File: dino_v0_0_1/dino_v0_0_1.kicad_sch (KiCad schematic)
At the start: 27 parts, among them Q1 Write Button Gate, U1 Quad AND

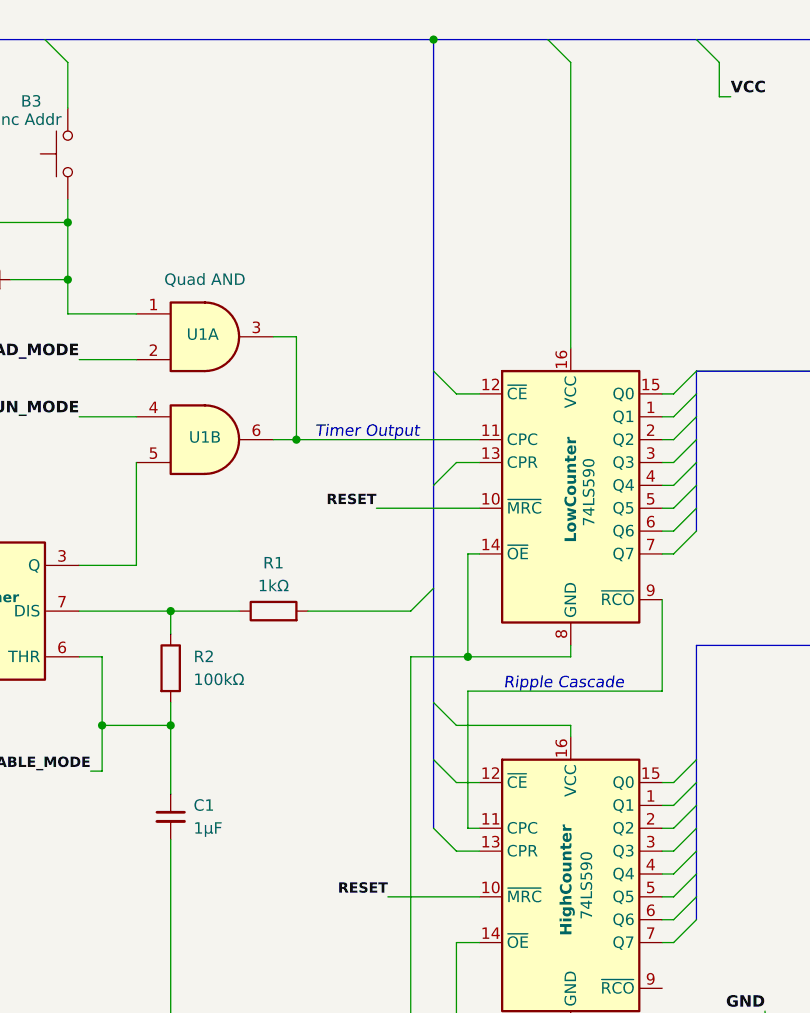
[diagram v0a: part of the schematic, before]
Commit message: Updates schematic connections and increments revision
Adjusts various schematic wire and bus connections for improved accuracy and clarity, removes obsolete bus entries, and adds new GND label and connection points. Increments schematic revision to v1.0.1. Replaces outdated PDF with updated version and resets project plot directory setting.

Enhances maintainability and correctness of the design.
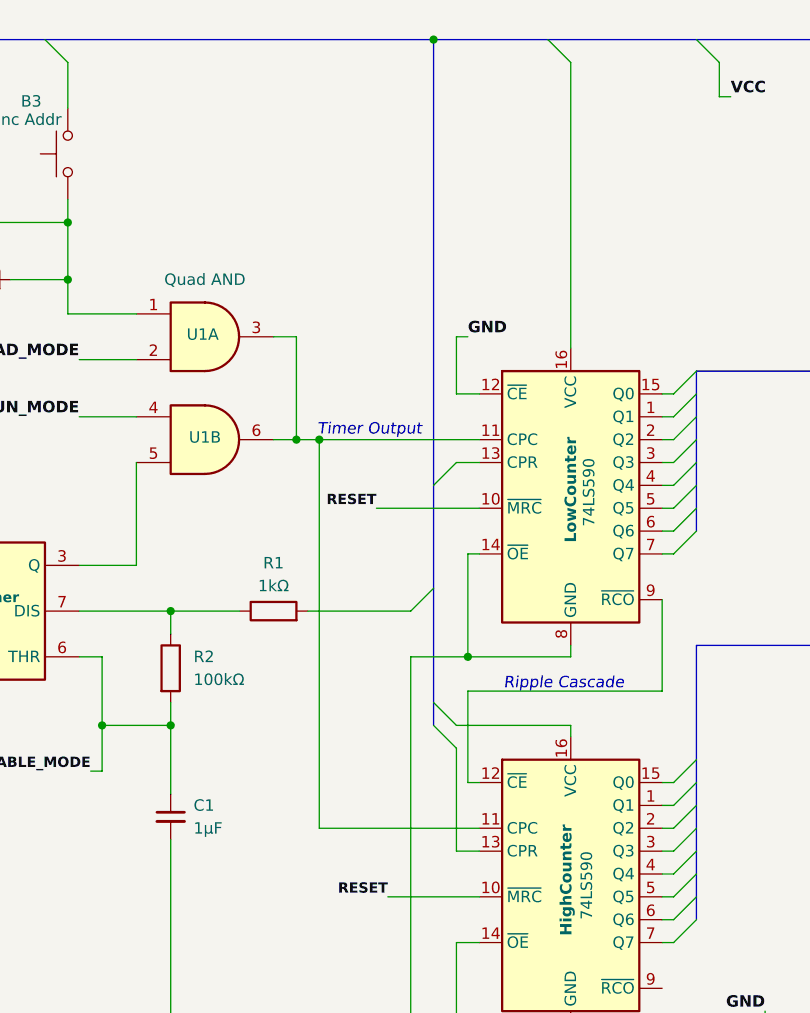
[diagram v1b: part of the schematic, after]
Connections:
- net GND: now also LowCounter.12 (~{CE})
- net at LowCounter.11 (CPC), U1.3, U1.6: now also HighCounter.11 (CPC)
- net at LowCounter.9 (~{RCO}): now also HighCounter.12 (~{CE}); no longer HighCounter.11 (CPC)
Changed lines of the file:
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@@
 		(title "Dino v0.0.1")
 		(date "2025-06-15")
-		(rev "v1.0.0")
+		(rev "v1.0.1")
 		(comment 1 "Core Components")
 		(comment 3 "Utilizes a 555 timer and binary counter to increment addressing.")
@@
 	(text "Timer Output"
 		(exclude_from_sim no)
-		(at 92.964 61.468 0)
+		(at 93.218 61.214 0)
 		(effects
 			(font
@@
 	)
 	(junction
+		(at 87.63 62.23)
+		(diameter 0)
+		(color 0 0 0 0)
+	)
+	(junction
 		(at 222.25 82.55)
 		(diameter 0)
@@
 	)
 	(bus_entry
-		(at 100.33 54.61)
-		(size 2.54 2.54)
-		(stroke
-			(width 0)
-			(type default)
-		)
-	)
-	(bus_entry
-		(at 100.33 105.41)
-		(size 2.54 2.54)
-		(stroke
-			(width 0)
-			(type default)
-		)
-	)
-	(bus_entry
 		(at 48.26 129.54)
 		(size -2.54 2.54)
@@
 	)
 	(bus_entry
-		(at 100.33 97.79)
-		(size 2.54 2.54)
-		(stroke
-			(width 0)
-			(type default)
-		)
-	)
-	(bus_entry
 		(at 127 59.69)
 		(size 2.54 -2.54)
@@
 		)
 	)
+	(bus_entry
+		(at 100.33 93.98)
+		(size 2.54 2.54)
+		(stroke
+			(width 0)
+			(type default)
+		)
+	)
 	(bus
 		(pts
@@
 	(bus
 		(pts
-			(xy 100.33 97.79) (xy 100.33 105.41)
+			(xy 100.33 91.44) (xy 100.33 93.98)
 		)
 		(stroke
@@
 	(wire
 		(pts
+			(xy 102.87 50.8) (xy 104.14 50.8)
+		)
+		(stroke
+			(width 0)
+			(type default)
+		)
+	)
+	(wire
+		(pts
 			(xy 149.86 60.96) (xy 151.13 60.96)
 		)
@@
 	(wire
 		(pts
-			(xy 104.14 90.17) (xy 104.14 105.41)
-		)
-		(stroke
-			(width 0)
-			(type default)
-		)
-	)
-	(wire
-		(pts
 			(xy 173.99 64.77) (xy 176.53 64.77)
 		)
@@
 	(wire
 		(pts
+			(xy 104.14 90.17) (xy 104.14 100.33)
+		)
+		(stroke
+			(width 0)
+			(type default)
+		)
+	)
+	(wire
+		(pts
 			(xy 199.39 86.36) (xy 201.93 86.36)
 		)
@@
 	(wire
 		(pts
+			(xy 104.14 100.33) (xy 105.41 100.33)
+		)
+		(stroke
+			(width 0)
+			(type default)
+		)
+	)
+	(wire
+		(pts
 			(xy 125.73 107.95) (xy 127 107.95)
 		)
@@
 		)
 	)
+	(wire
+		(pts
+			(xy 87.63 105.41) (xy 105.41 105.41)
+		)
+		(stroke
+			(width 0)
+			(type default)
+		)
+	)
 	(bus
 		(pts
@@
 		)
 	)
-	(bus
-		(pts
-			(xy 100.33 91.44) (xy 100.33 97.79)
-		)
-		(stroke
-			(width 0)
-			(type default)
-			(color 194 0 0 1)
-		)
-	)
 	(wire
 		(pts
@@
 		)
 	)
-	(bus
+	(wire
 		(pts
-			(xy 147.32 62.23) (xy 147.32 66.04)
+			(xy 87.63 62.23) (xy 87.63 105.41)
 		)
 		(stroke
@@
 		)
 	)
-	(wire
+	(bus
 		(pts
-			(xy 204.47 119.38) (xy 204.47 109.22)
+			(xy 147.32 62.23) (xy 147.32 66.04)
 		)
 		(stroke
@@
 	(wire
 		(pts
-			(xy 125.73 105.41) (xy 127 105.41)
+			(xy 204.47 119.38) (xy 204.47 109.22)
 		)
 		(stroke
@@
 	(wire
 		(pts
-			(xy 234.95 49.53) (xy 237.49 49.53)
+			(xy 125.73 105.41) (xy 127 105.41)
 		)
 		(stroke
@@
 	(wire
 		(pts
-			(xy 234.95 52.07) (xy 237.49 52.07)
+			(xy 234.95 49.53) (xy 237.49 49.53)
 		)
 		(stroke
@@
 	(wire
 		(pts
-			(xy 187.96 110.49) (xy 194.31 110.49)
+			(xy 234.95 52.07) (xy 237.49 52.07)
 		)
 		(stroke
@@
 	(wire
 		(pts
-			(xy 104.14 105.41) (xy 105.41 105.41)
+			(xy 187.96 110.49) (xy 194.31 110.49)
 		)
 		(stroke
@@
 	(wire
 		(pts
-			(xy 85.09 62.23) (xy 105.41 62.23)
+			(xy 85.09 62.23) (xy 87.63 62.23)
 		)
 		(stroke
@@
 	(wire
 		(pts
-			(xy 102.87 100.33) (xy 105.41 100.33)
-		)
-		(stroke
-			(width 0)
-			(type default)
-		)
-	)
-	(wire
-		(pts
 			(xy 125.73 74.93) (xy 127 74.93)
 		)
@@
 		)
 	)
-	(bus
-		(pts
-			(xy 100.33 17.78) (xy 100.33 54.61)
-		)
-		(stroke
-			(width 0)
-			(type default)
-			(color 194 0 0 1)
-		)
-	)
 	(wire
 		(pts
@@
 		)
 	)
+	(wire
+		(pts
+			(xy 102.87 57.15) (xy 102.87 50.8)
+		)
+		(stroke
+			(width 0)
+			(type default)
+		)
+	)
 	(bus
 		(pts
@@
 	(wire
 		(pts
+			(xy 87.63 62.23) (xy 105.41 62.23)
+		)
+		(stroke
+			(width 0)
+			(type default)
+		)
+	)
+	(wire
+		(pts
 			(xy 49.53 20.32) (xy 49.53 31.75)
 		)
@@
 	(bus
 		(pts
-			(xy 100.33 54.61) (xy 100.33 67.31)
+			(xy 100.33 17.78) (xy 100.33 67.31)
 		)
 		(stroke
@@
 	(wire
 		(pts
+			(xy 102.87 96.52) (xy 102.87 107.95)
+		)
+		(stroke
+			(width 0)
+			(type default)
+		)
+	)
+	(wire
+		(pts
 			(xy 185.42 72.39) (xy 209.55 72.39)
 		)
@@
 			)
 			(justify left bottom)
+		)
+	)
+	(label "GND"
+		(at 104.14 50.8 0)
+		(effects
+			(font
+				(size 1.27 1.27)
+				(thickness 0.254)
+				(bold yes)
+				(color 0 0 0 1)
+			)
+			(justify left bottom)

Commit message: Revises schematic wiring and junctions for improved clarity
Adjusts wire routing and junctions in the schematic for clearer connectivity, including adding new junctions and wires, and removing unused or redundant bus entries and connections. Updates plot directory in project settings and adds an auto-save tracking file.

Enhances schematic readability and maintains project organization.
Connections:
- net at HighCounter.11 (CPC), LowCounter.11 (CPC), U1.3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: now also HighCounter.13 (CPR), LowCounter.13 (CPR)
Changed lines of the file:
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@@
 	)
 	(junction
+		(at 102.87 62.23)
+		(diameter 0)
+		(color 0 0 0 0)
+	)
+	(junction
 		(at 222.25 39.37)
 		(diameter 0)
@@
 	)
 	(junction
+		(at 102.87 105.41)
+		(diameter 0)
+		(color 0 0 0 0)
+	)
+	(junction
 		(at 44.45 44.45)
 		(diameter 0)
@@
 	)
 	(bus_entry
-		(at 102.87 64.77)
-		(size -2.54 2.54)
-		(stroke
-			(width 0)
-			(type default)
-		)
-	)
-	(bus_entry
 		(at 40.64 132.08)
 		(size 2.54 2.54)
@@
 		)
 	)
-	(bus_entry
-		(at 100.33 93.98)
-		(size 2.54 2.54)
-		(stroke
-			(width 0)
-			(type default)
-		)
-	)
 	(bus
 		(pts
@@
 		)
 	)
+	(wire
+		(pts
+			(xy 102.87 105.41) (xy 102.87 107.95)
+		)
+		(stroke
+			(width 0)
+			(type default)
+		)
+	)
 	(bus
 		(pts
@@
 	(bus
 		(pts
-			(xy 100.33 67.31) (xy 100.33 78.74)
+			(xy 100.33 17.78) (xy 100.33 78.74)
 		)
 		(stroke
@@
 		)
 	)
+	(wire
+		(pts
+			(xy 102.87 105.41) (xy 105.41 105.41)
+		)
+		(stroke
+			(width 0)
+			(type default)
+		)
+	)
 	(bus
 		(pts
@@
 	(wire
 		(pts
-			(xy 87.63 105.41) (xy 105.41 105.41)
+			(xy 87.63 105.41) (xy 102.87 105.41)
 		)
 		(stroke
@@
 	(wire
 		(pts
+			(xy 102.87 62.23) (xy 102.87 64.77)
+		)
+		(stroke
+			(width 0)
+			(type default)
+		)
+	)
+	(wire
+		(pts
 			(xy 234.95 54.61) (xy 237.49 54.61)
 		)
@@
 	(wire
 		(pts
-			(xy 87.63 62.23) (xy 105.41 62.23)
+			(xy 87.63 62.23) (xy 102.87 62.23)
 		)
 		(stroke
@@
 		)
 	)
-	(bus
+	(wire
 		(pts
-			(xy 100.33 17.78) (xy 100.33 67.31)
+			(xy 132.08 20.32) (xy 132.08 24.13)
 		)
 		(stroke
 			(width 0)
 			(type default)
-			(color 194 0 0 1)
 		)
 	)
-	(wire
+	(bus
 		(pts
-			(xy 132.08 20.32) (xy 132.08 24.13)
+			(xy 129.54 85.09) (xy 129.54 97.79)
 		)
 		(stroke
@@
 		)
 	)
-	(bus
+	(wire
 		(pts
-			(xy 129.54 85.09) (xy 129.54 97.79)
+			(xy 207.01 46.99) (xy 209.55 46.99)
 		)
 		(stroke
@@
 	(wire
 		(pts
-			(xy 207.01 46.99) (xy 209.55 46.99)
+			(xy 102.87 62.23) (xy 105.41 62.23)
 		)
 		(stroke
@@
 		)
 		(stroke
-			(width 0)
-			(type default)
-		)
-	)
-	(wire
-		(pts
-			(xy 102.87 96.52) (xy 102.87 107.95)
-		)
-		(stroke

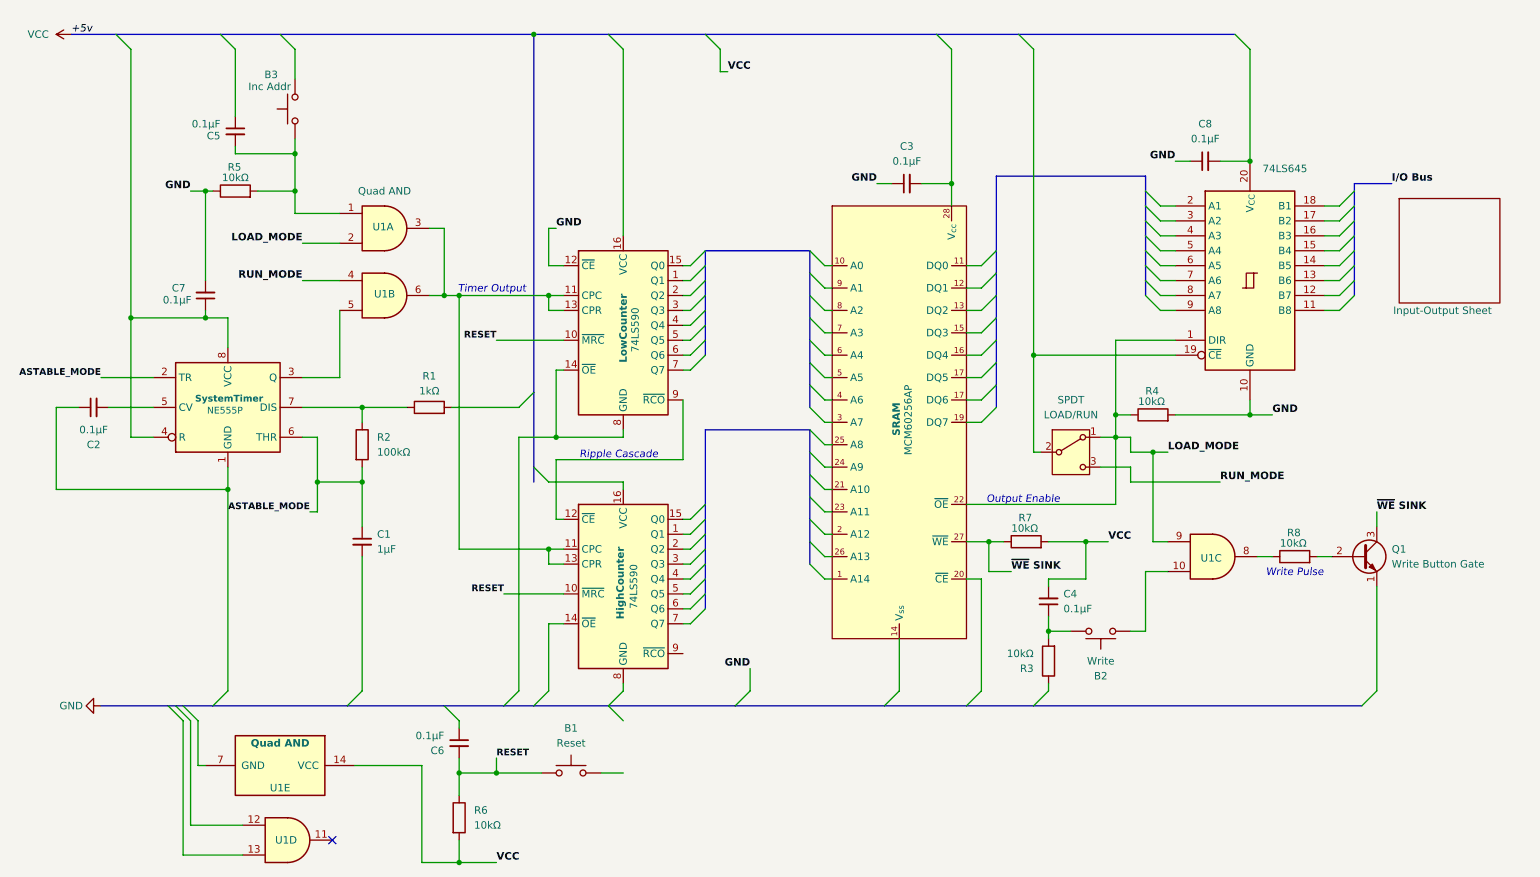
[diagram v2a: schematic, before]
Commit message: Updates schematic with corrections
- Corrects ~CE on 74LS645
- Fixes MCM60256AP DQ6 Pin Number
- Removes "Net Label" for +5V and adds correct text label
- Attaches both GND and VCC to bus proper
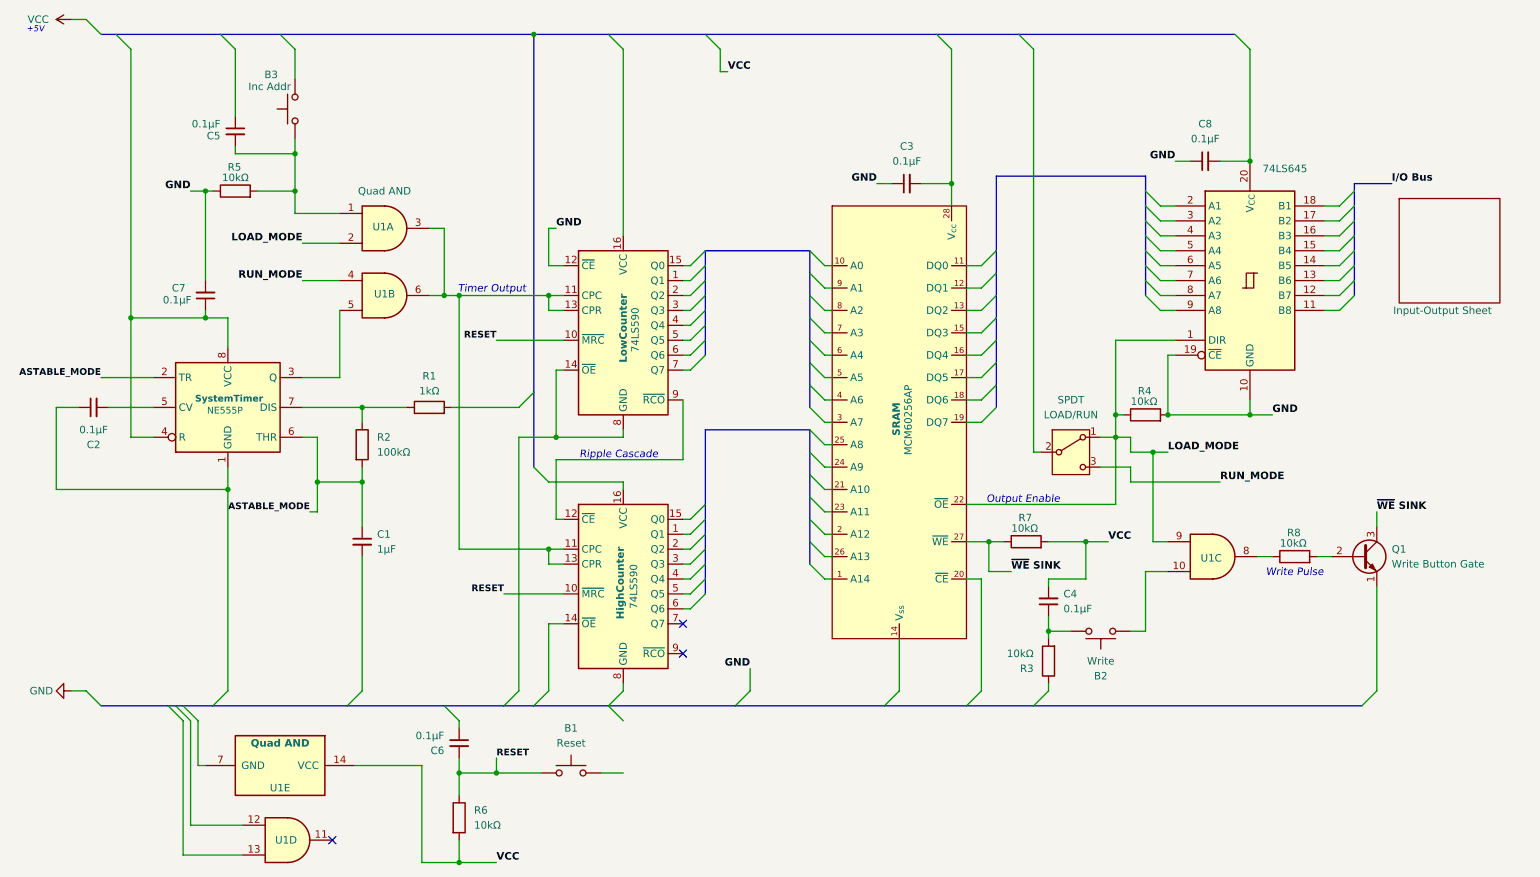
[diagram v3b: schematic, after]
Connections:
- net GND: now also 74LS645.19 (~{CE})
- net at SPDT.2 (B): no longer 74LS645.19 (~{CE})
- no-connect marks 1 -> 3
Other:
- note added: "+5V"
- moved on the sheet: R4
